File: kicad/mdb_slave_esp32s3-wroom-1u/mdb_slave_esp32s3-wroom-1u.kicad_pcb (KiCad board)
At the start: 2 copper layers, 127.5 x 79 mm, 66 parts, among them J1 USB_C_Receptacle_USB2.0_16P, J10 Conn_01x04_Pin_JST, J11 Screw_Terminal_01x03, J12 MDB_Connector, J13 Screw_Terminal_01x03, J14 Screw_Terminal_01x03, J2 Screw_Terminal_01x02, J3 Screw_Terminal_01x02, J4 Screw_Terminal_01x03, J5 Screw_Terminal_01x03, J6 Screw_Terminal_01x03, J7 Conn_01x06_Pin, J8 Conn_01x03_Pin_JST, J9 Conn_01x04_Pin, Q1 MMBT3904, Q2 MMBT3904, Q3 MMBT3904, SW1 SW_Push, U1 ESP32-S3-WROOM-1U-N16R2, U2 AP63203QWU-7, U3 TLP785, U4 TLP785

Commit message: fix(wroom-1u): correct board designator esp32s3-wroom-u1 -> esp32s3-wroom-1u
The module is actually named ESP32-S3-WROOM-1U, not "WROOM-U1" (digit/letter
order was swapped). Renames the KiCad project directory and its three
project files (.kicad_pro/.kicad_sch/.kicad_pcb), updates the embedded
project-name references inside them (sheet paths, instance paths), and
corrects the bottom-silkscreen text that gets printed on the physical board.
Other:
- board text added: "mdb-slave-esp32s3-wroom-1u"
- board text removed: "mdb-slave-esp32s3-wroom-u1"

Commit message: feat(wroom-1u): update PCB to rev1.2 (fully routed) and sync README
Board is now fully routed and fabrication-ready. README updated to
reflect rev1.2 status, the current connector reference designators
(J1-J3, P1-P8, H1), and functional blocks, replacing the stale
"not started" rev1.0 content and outdated J1-J14 connector table.
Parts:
- removed F1: 1.1A (33V), Fuse:Fuse_1812_4532Metric
- removed J10: Conn_01x04_Pin_JST, Connector_JST:JST_PH_B4B-PH-K_1x04_P2.00mm_Vertical
- removed J11, J13, J14, J4, J5, J6: Screw_Terminal_01x03, EasyEDA2Kicad:CONN-TH_3P-P2.54_DIBO_DB141R-2.54-3P
- removed J12: MDB_Connector, Connector_Molex:Molex_Mini-Fit_Jr_5566-06A_2x03_P4.20mm_Vertical
- removed J7: Conn_01x06_Pin, Connector_PinHeader_2.54mm:PinHeader_1x06_P2.54mm_Vertical
- removed J8: Conn_01x03_Pin_JST, Connector_JST:JST_PH_B3B-PH-K_1x03_P2.00mm_Vertical
- removed J9: Conn_01x04_Pin, Connector_PinHeader_2.54mm:PinHeader_1x04_P2.54mm_Vertical
- removed R23: 10k, Resistor_SMD:R_0603_1608Metric
- removed SW1: SW_Push, Button_Switch_SMD:SW_Tactile_SPST_NO_Straight_CK_PTS636Sx25SMTRLFS
- removed U2: AP63203QWU-7, Package_TO_SOT_SMD:TSOT-23-6
- removed U3, U4: TLP785, EasyEDA2Kicad:SMD-4_L4.6-W3.7-P2.54-LS7.0-BR
- added B1: Btn1, Global Libraries:KEY-SMD_B3U-1000PM, F.Cu at (85.3, 121.1)
- added B2: Btn1, Global Libraries:KEY-SMD_B3U-1000PM, F.Cu at (85.3, 124.2)
- added C10: 10uF, Capacitor_SMD:C_0603_1608Metric, F.Cu at (84.2, 141.5)
- added C11: 100nF, Capacitor_SMD:C_0603_1608Metric, F.Cu at (82.7, 141.5)
- added C12: 100nF, Capacitor_SMD:C_0603_1608Metric, F.Cu at (103.0, 136.2)
- added C7: 100nF, Capacitor_SMD:C_0603_1608Metric, F.Cu at (90.3, 148.9)
- added C8: 22uF, Capacitor_SMD:C_0603_1608Metric, F.Cu at (90.4, 142.3)
- added C9: 22uF, Capacitor_SMD:C_0603_1608Metric, F.Cu at (90.4, 140.8)
- added F2: Polyfuse, Capacitor_SMD:C_1812_4532Metric, F.Cu at (183.4, 143.5)
- added G***: LOGO, LOGO, B.Cu at (92.5, 122.0)
- added H10: Buzzer_OUT, TestPoint:TestPoint_Pad_D1.0mm, B.Cu at (127.7, 134.6)
- added H6: +5V, TestPoint:TestPoint_Pad_D1.0mm, B.Cu at (82.5, 141.6)
- added H7: +3V3, TestPoint:TestPoint_Pad_D1.0mm, B.Cu at (89.8, 144.8)
- added H8: DO, TestPoint:TestPoint_Pad_D1.0mm, F.Cu at (109.1, 136.2)
- added H9: Buzzer_IN, TestPoint:TestPoint_Pad_D1.0mm, B.Cu at (113.2, 136.2)
- added LED1: XL-2121RGBC-2812B, Global Libraries:LED-SMD_4P-L2.1-W2.1-BR_XL-2121RGBC-WS2812B_C5349957, F.Cu at (106.2, 135.7)
- added P1: WJ500V-5.08-3P-14-00A, Global Libraries:CONN-TH_3P-P5.00_WJ500V-5.08-3P_C72334, F.Cu at (183.5, 118.6)
- added P2: WJ500V-5.08-3P-14-00A, Global Libraries:CONN-TH_3P-P5.00_WJ500V-5.08-3P_C72334, F.Cu at (168.0, 118.6)
- added P3: WJ500V-5.08-3P-14-00A, Global Libraries:CONN-TH_3P-P5.00_WJ500V-5.08-3P_C72334, F.Cu at (147.8, 145.9)
- added P4: WJ500V-5.08-3P-14-00A, Global Libraries:CONN-TH_3P-P5.00_WJ500V-5.08-3P_C72334, F.Cu at (101.2, 145.9)
- added P5: WJ500V-5.08-3P-14-00A, Global Libraries:CONN-TH_3P-P5.00_WJ500V-5.08-3P_C72334, F.Cu at (116.7, 145.9)
- added P6: WJ500V-5.08-3P-14-00A, Global Libraries:CONN-TH_3P-P5.00_WJ500V-5.08-3P_C72334, F.Cu at (132.3, 145.9)
- added P7: WJ500V-5.08-2P-14-00A, Global Libraries:CONN-TH_2P-P5.00_WJ500V-5.08-2P_C8465, F.Cu at (196.5, 128.1)
- added P8: WJ500V-5.08-2P-14-00A, Global Libraries:CONN-TH_2P-P5.00_WJ500V-5.08-2P_C8465, F.Cu at (196.5, 138.6)
- added U5: TLP785, Global Libraries:SMD-4_L4.6-W6.5-P2.54-LS10.2-BR_C45445, F.Cu at (138.5, 134.2)
- added U6: TLP785, Global Libraries:SMD-4_L4.6-W6.5-P2.54-LS10.2-BR_C45445, F.Cu at (138.5, 127.6)
- added U8: AP63203QWU-7, Package_TO_SOT_SMD:TSOT-23-6, F.Cu at (88.7, 145.3)
- added USBC1: TYPE-C-31-M-12, Global Libraries:USB-C_SMD-TYPE-C-31-M-12, F.Cu at (83.3, 131.9)
- BUZZER1: footprint easyeda2kicad:BUZ-SMD_4P-L8.5-W8.5-P8.50-BR -> Global Libraries:BUZ-SMD_4P-L8.5-W8.5-P8.50-BR_C94599
- C5: value 22uF -> 100nF
- C6: value 22uF -> 10uF
- D1: value Schottky 60V/1A -> 1N4148WS; footprint Diode_SMD:D_SOD-123 -> Diode_SMD:D_SOD-323
- D2: value XL-2121RGBC-2812B -> 1N4148WS; footprint LED_SMD:LED_WS2812B-2020_PLCC4_2.0x2.0mm -> Diode_SMD:D_SOD-323
- D3: value Schottky 30V/500mA -> BAT760-7; footprint Diode_SMD:D_SOD-123 -> Diode_SMD:D_SOD-323
- D4: value Schottky 30V/500mA -> 1N4148WS; footprint Diode_SMD:D_SOD-123 -> Diode_SMD:D_SOD-323
- D5, D6: value 1N4148WS -> BAT760-7
- H1: value MountingHole2.5 -> HC-5557-2*3AW; footprint MountingHole:MountingHole_2.5mm -> Global Libraries:CONN-TH_6P-P4.20-S5.50_5557-2X3AW_C2845788
- H2, H3, H4, H5: value MountingHole2.5 -> MountingHole; footprint MountingHole:MountingHole_2.5mm -> MountingHole:MountingHole_2.7mm_M2.5_ISO7380
- J1: value USB_C_Receptacle_USB2.0_16P -> Conn_01x06_Pin; footprint Connector_USB:USB_C_Receptacle_G-Switch_GT-USB-7010ASV -> Connector_PinSocket_2.54mm:PinSocket_1x06_P2.54mm_Vertical
- J2: value Screw_Terminal_01x02 -> Conn_01x06_Pin; footprint EasyEDA2Kicad:CONN-TH_2P-P2.54_DIBO_DB141R-2.54-2P -> Connector_PinSocket_2.54mm:PinSocket_1x06_P2.54mm_Vertical
- J3: value Screw_Terminal_01x02 -> Conn_01x04_Pin; footprint EasyEDA2Kicad:CONN-TH_2P-P2.54_DIBO_DB141R-2.54-2P -> Connector_JST:JST_XH_B4B-XH-A_1x04_P2.50mm_Vertical
- L1: footprint Inductor_SMD:L_TechFuse_SL0420 -> Inductor_SMD:L_0603_1608Metric
- R1, R17, R2: value 10k -> 10KΩ
- R10, R20: value 1k -> 10KΩ
- R11, R8: value 4.7k -> 4.7KΩ
- R12: value 100ohm -> 470Ω
- R13: value 4.7k -> 10KΩ
- R14, R15: value 4.7k -> 1KΩ
- R16: value 4.7k -> 470Ω
- R18: value 470ohm -> 10KΩ
- R19: value 10k -> 1KΩ
- R21: value 470ohm -> 5.1KΩ
- R22: value 10k -> 5.1KΩ
- R3: value 5.1k -> 470Ω
- R4: value 5.1k -> 4.7KΩ
- R5, R6: value 10k -> 0R; footprint Resistor_SMD:R_0603_1608Metric -> Resistor_SMD:R_0603_1608Metric_Pad0.98x0.95mm_HandSolder
- R7: value 10k -> 4.7KΩ
- R9: value 1k -> 4.7KΩ
- TH1: footprint Resistor_SMD:R_0603_1608Metric -> Capacitor_SMD:C_0603_1608Metric_Pad1.08x0.95mm_HandSolder
- U1: footprint EasyEDA2Kicad:WIRELM-SMD_ESP32-S3-WROOM-1U -> Global Libraries:WIRELM-SMD_ESP32-S3-WROOM-1U_C3013945
- moved H3 263.5 mm to (82.5, 116.5)
- moved H2 245.7 mm to (82.5, 148.0)
- moved D6 162.2 mm to (85.9, 141.6), turned to 90 degrees
- moved H5 148.1 mm to (198.8, 116.5)
- moved H1 142.3 mm to (170.9, 135.0)
- moved H4 134.5 mm to (198.8, 148.0)
- moved R17 123.5 mm to (177.5, 124.9), turned to 180 degrees
- moved R19 115.1 mm to (180.6, 130.5), turned to -90 degrees
- moved Q1 111.7 mm to (128.9, 130.6), turned to -90 degrees
- moved D1 108.4 mm to (120.3, 134.6)
- moved L1 103.4 mm to (88.7, 148.9), turned to -90 degrees
- moved BUZZER1 99.9 mm to (120.4, 127.9)
- moved R9 96.7 mm to (152.9, 120.8), turned to 180 degrees
- moved C6 96.5 mm to (87.8, 141.6), turned to 90 degrees
- moved J1 95.3 mm to (114.4, 114.8), turned to 90 degrees
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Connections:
- net /io6 renamed GPIO6
- BUZZER1 pad 2: GND -> Net-(BUZZER1-Pad2)
- C1 pad 1: GND -> EN
- C1 pad 2: +3V3 -> GND
- C3 pad 1: /vin -> GND
- C3 pad 2: Net-(U2-IN) -> +3V3
- C4 pad 1: Net-(U2-BST) -> EN
- C4 pad 2: Net-(U2-SW) -> GND
- C5 pad 1: +3V3 -> IO0
- C6 pad 1: +3V3 -> +5V
- D1 pad 1: /vin -> +3V3
- D2 pad 1: unconnected-(D2-DOUT-Pad1) -> Net-(D2-K)
- D2 pad 2: GND -> Net-(D2-A)
- D4 pad 1: +3V3 -> Net-(D4-K)
- D5 pad 1: Net-(D5-K) -> +3V3
- D6 pad 1: Net-(D6-K) -> +5V
- J2 pad 1: Net-(D3-A) -> /MTMS
- J2 pad 2: +3V3 -> /MTDI
- J3 pad 1: Net-(D4-A) -> GND
- L1 pad 1: Net-(U2-SW) -> Net-(U8-SW)
- Q1 pad 3: Net-(D3-A) -> Net-(D1-A)
- Q2 pad 3: Net-(D4-A) -> Net-(D3-A)
- Q3 pad 3: Net-(J8-Pin_3) -> Net-(D5-A)
- R1 pad 1: /boot -> +3V3
- R1 pad 2: +3V3 -> EN
- R10 pad 1: Net-(Q2-B) -> +3V3
- R10 pad 2: /io2 -> IO0
- R11 pad 2: /io15 -> GPIO15
- R12 pad 1: Net-(BUZZER1-+) -> /mdb_master_transmit
- R12 pad 2: /io12 -> Net-(D2-A)
- R13 pad 1: /io16 -> GPIO7
- R14 pad 1: /io13 -> +3V3
- R14 pad 2: Net-(Q3-B) -> GPIO4
- R15 pad 1: /io11 -> Net-(Q2-B)
- R15 pad 2: +3V3 -> GPIO2
- R16 pad 1: /io10 -> Net-(D4-A)
- R18 pad 1: Net-(D5-A) -> GPIO17
- R18 pad 2: /mdb_master_transmit -> +3V3
- R19 pad 1: /io47 -> Net-(Q3-B)
- R19 pad 2: +3V3 -> GPIO1
- R2 pad 1: +3V3 -> Net-(U1-IO3)
- R2 pad 2: Net-(U1-EN) -> GND
- R20 pad 1: +3V3 -> GPIO18
- R20 pad 2: /io4 -> +3V3
- R21 pad 1: +3V3 -> Net-(USBC1-CC1)
- R21 pad 2: Net-(D6-A) -> GND
- R22 pad 1: /io48 -> Net-(USBC1-CC2)
- R22 pad 2: +3V3 -> GND
- R3 pad 1: Net-(J1-CC2) -> GPIO12
- R3 pad 2: GND -> Net-(Q1-B)
- R4 pad 1: Net-(J1-CC1) -> +3V3
- R4 pad 2: GND -> GPIO15
- R5 pad 1: Net-(U1-IO46) -> +3V3
- R5 pad 2: GND -> Net-(BUZZER1-+)
- R6 pad 1: Net-(U1-IO45) -> Net-(D1-A)
- R6 pad 2: GND -> Net-(BUZZER1-Pad2)
- R7 pad 1: /io7 -> +3V3
- R7 pad 2: +3V3 -> GPIO16
- R8 pad 1: /io15 -> GPIO10_SDA
- R9 pad 1: Net-(Q1-B) -> GPIO11_SCL
- R9 pad 2: /io1 -> +3V3
- TH1 pad 1: GND -> GPIO7
- TH1 pad 2: /io7 -> GND
- U1 pad 10: unconnected-(U1-IO17-Pad10) -> GPIO17
- U1 pad 11: unconnected-(U1-IO18-Pad11) -> GPIO18
- U1 pad 13: /usb- -> USB_D-
- U1 pad 14: /usb+ -> USB_D+
- U1 pad 16: Net-(U1-IO46) -> unconnected-(U1-IO46-Pad16)
- U1 pad 18: /io10 -> GPIO10_SDA
- U1 pad 19: /io11 -> GPIO11_SCL
- U1 pad 20: /io12 -> GPIO12
- U1 pad 21: /io13 -> unconnected-(U1-IO13-Pad21)
- U1 pad 23: /io21 -> GPIO21
- U1 pad 24: /io47 -> unconnected-(U1-IO47-Pad24)
- U1 pad 25: /io48 -> unconnected-(U1-IO48-Pad25)
- U1 pad 26: Net-(U1-IO45) -> unconnected-(U1-IO45-Pad26)
- U1 pad 27: /boot -> IO0
- U1 pad 3: Net-(U1-EN) -> EN
- U1 pad 32: /io39 -> /MTCk
- U1 pad 33: /io40 -> /MTDO
- U1 pad 34: /io41 -> /MTDI
- U1 pad 35: /io42 -> /MTMS
- U1 pad 36: /u0rxd -> /RXD
- U1 pad 37: /u0txd -> /TXD
- U1 pad 38: /io2 -> GPIO2
- U1 pad 39: /io1 -> GPIO1
- U1 pad 4: /io4 -> GPIO4
- U1 pad 5: /io5 -> GPIO5
- U1 pad 7: /io7 -> GPIO7
- U1 pad 8: /io15 -> GPIO15
- U1 pad 9: /io16 -> GPIO16
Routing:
- net +3V3: track 0.00 -> 436.9 mm, vias 0 -> 9
- net +5V: track 0.00 -> 120.8 mm, vias 0 -> 2
- net GPIO6: track 0.00 -> 116.0 mm, vias 0 -> 1
- net GPIO15: track 0.00 -> 100.2 mm, vias 0 -> 2
- net GPIO17: track 0.00 -> 98.8 mm, vias 0 -> 2
- net GPIO18: track 0.00 -> 89.5 mm, vias 0 -> 2
- net GPIO10_SDA: track 0.00 -> 82.8 mm, vias 0 -> 2
- net GPIO2: track 0.00 -> 80.8 mm, vias 0 -> 2
- net GPIO11_SCL: track 0.00 -> 77.6 mm, vias 0 -> 2
- net GPIO1: track 0.00 -> 75.8 mm, vias 0 -> 2
- net IO0: track 0.00 -> 64.5 mm, vias 0 -> 4
- net /mdb_master_receive: track 0.00 -> 58.0 mm
- net /mdb_communications_common: track 0.00 -> 55.8 mm
- net GPIO5: track 0.00 -> 52.2 mm, vias 0 -> 2
- net GPIO4: track 0.00 -> 50.9 mm, vias 0 -> 2
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- added copper zone on B.Cu, net GND
- added copper zone on F.Cu, net GND
- added copper zone on In1.Cu, net GND
- added copper zone on In2.Cu, net GND
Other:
- board size 127.5 x 79 mm -> 123.2 x 38.5 mm
- copper layers 2 -> 4
- board text added: "0/BOOT"
- board text added: "1-WIRE BUS#1"
- board text added: "1-WIRE BUS#2"
- board text added: "123.2 mm"
- board text added: "38.5 mm"
- board text added: "3V3"
- board text added: "3v3"
- board text added: "5V"
- board text added: "Buzzer OUT"
- board text added: "CUST. IN #1"
- board text added: "CUST. IN #2"
- board text added: "CUST. IN #3"
- board text added: "EN"
- board text added: "GND"
- board text added: "GPIO15"
- board text added: "GPIO16"
- board text added: "GPIO17"
- board text added: "GPIO18"
- board text added: "GPIO6"
- board text added: "I2C"
- board text added: "IN"
- board text added: "IO0"
- board text added: "JTAG"
- board text added: "LED DO"
- board text added: "MDB"
- board text added: "MDB-ESP32-CASHLESS WROOM-1U BOARD"
- board text added: "MD_C"
- board text added: "MD_R"
- board text added: "MD_T"
- board text added: "MTCK"
- board text added: "MTDI"
- board text added: "MTDO"
- board text added: "MTMS"
- board text added: "RELAY #1"
- board text added: "RELAY #2"
- board text added: "REV 1.2"
- board text added: "RST"
- board text added: "RXD"
- board text added: "SCL"
- board text added: "SDA"
- board text added: "TXD"
- board text added: "UART DEBUG"
- board text added: "VIN"
- board text added: "X"
- board text removed: "commit xxxxxxx"
- board text removed: "mdb-slave-esp32s3-wroom-1u"

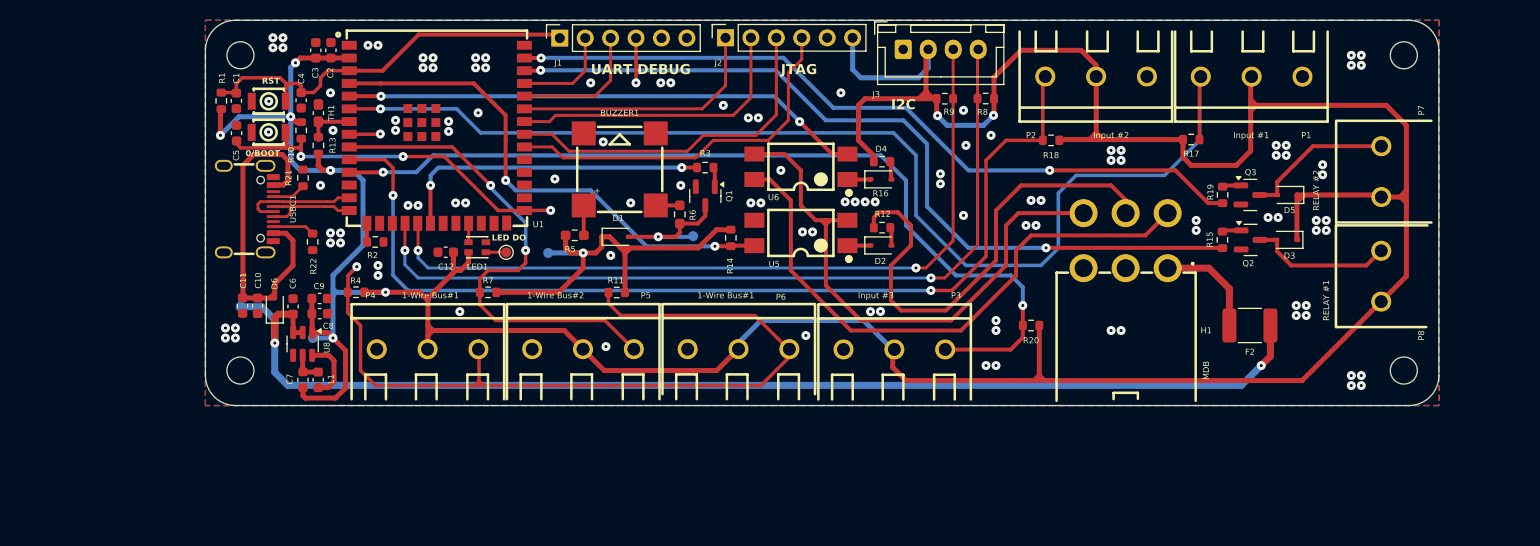
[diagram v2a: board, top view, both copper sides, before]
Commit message: feat(wroom-1u): update PCB to rev1.3 (15A relay upgrade) and add fabrication gerbers
- Relay outputs redesigned: SRD-03VDC-SL-C 15A-class relays (K2/K3) driven
  low-side by MMBT3904 (Q2/Q3) with 1N4148WS flyback diodes, switched
  through TLP785 optocouplers (U4/U5) for GPIO isolation
- README rewritten to match rev1.3: updated reference designators, honest
  status section (4 minor ERC items, PCB/schematic re-sync pending),
  known relay drive-logic inversion documented as an open point
- Add gerber_to_order/ (JLCPCB, PCBWay) fabrication archives, versioned via
  .gitignore whitelist update

Note: PCB/schematic parity re-sync (reference renumbering from the relay
stage addition) and a voltage regulator issue are still open, handed off
to the hardware engineer for follow-up before ordering.
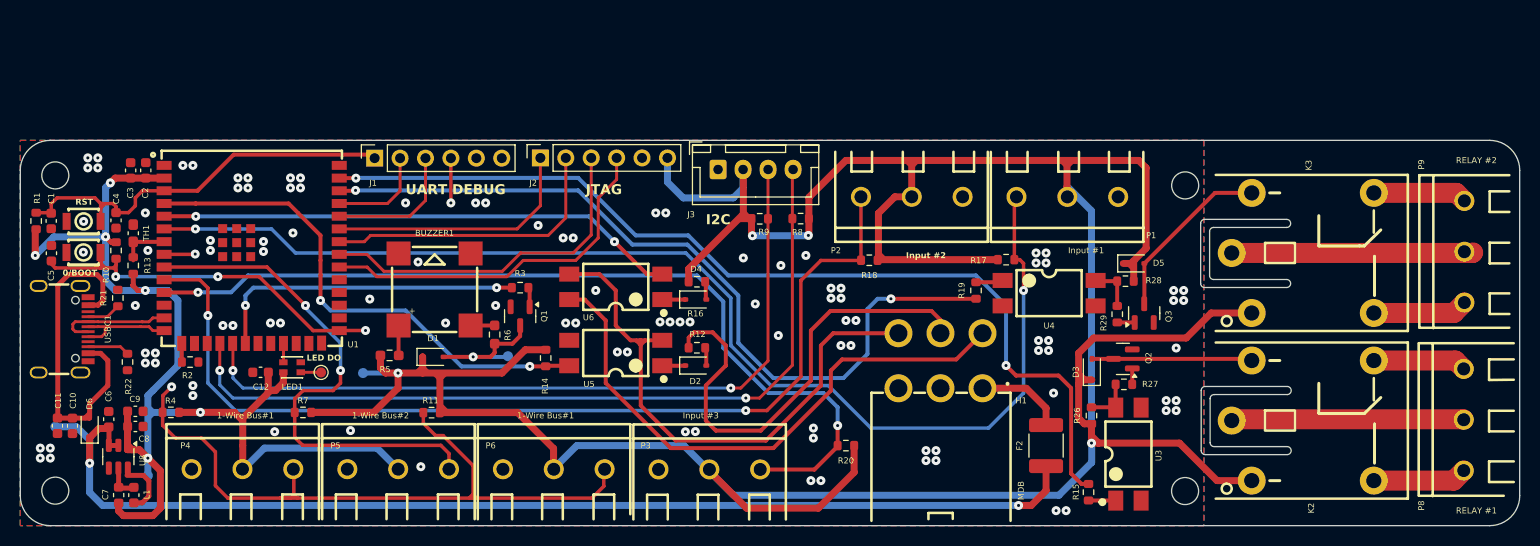
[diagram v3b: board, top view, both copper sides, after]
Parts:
- removed P7: WJ500V-5.08-2P-14-00A, Global Libraries:CONN-TH_2P-P5.00_WJ500V-5.08-2P_C8465
- added K2: SRD-03VDC-SL-C, Global Libraries:RELAY-TH_SRD-XXVDC-XL-C_C24585, F.Cu at (188.6, 153.0)
- added K3: SRD-03VDC-SL-C, Global Libraries:RELAY-TH_SRD-XXVDC-XL-C_C24585, F.Cu at (188.6, 136.3)
- added P9: WJ500V-5.08-3P-14-00A, Global Libraries:CONN-TH_3P-P5.00_WJ500V-5.08-3P_C72334, F.Cu at (204.8, 136.1)
- added R26: 10KΩ, Resistor_SMD:R_0603_1608Metric, F.Cu at (167.5, 152.5)
- added R27: 100Ω, Resistor_SMD:R_0603_1608Metric, F.Cu at (170.8, 149.4)
- added R28: 10KΩ, Resistor_SMD:R_0603_1608Metric, F.Cu at (170.9, 139.1)
- added R29: 100Ω, Resistor_SMD:R_0603_1608Metric, F.Cu at (170.1, 142.4)
- added U3: TLP785, Global Libraries:SMD-4_L4.6-W6.5-P2.54-LS10.2-BR_C45445, F.Cu at (171.2, 156.3)
- added U4: TLP785, Global Libraries:SMD-4_L4.6-W6.5-P2.54-LS10.2-BR_C45445, F.Cu at (163.3, 140.3)
- D3, D5: value BAT760-7 -> 1N4148WS
- P8: value WJ500V-5.08-2P-14-00A -> WJ500V-5.08-3P-14-00A; footprint Global Libraries:CONN-TH_2P-P5.00_WJ500V-5.08-2P_C8465 -> Global Libraries:CONN-TH_3P-P5.00_WJ500V-5.08-3P_C72334
- R15, R19: value 1KΩ -> 270Ω
- moved R15 28.5 mm to (167.2, 160.2)
- moved R19 26.4 mm to (156.0, 140.0), turned to 90 degrees
- moved H5 25.4 mm to (176.9, 129.5)
- moved H4 25.0 mm to (176.9, 160.0)
- moved F2 23.6 mm to (163.0, 155.5), turned to 90 degrees
- moved D3 23.4 mm to (167.6, 147.9), turned to 90 degrees
- moved G*** 23.4 mm to (72.8, 134.6)
- moved R3 22.1 mm to (110.4, 139.7)
- moved BUZZER1 22.1 mm to (101.9, 139.9)
- moved C3 22.1 mm to (71.5, 128.0)
- moved R17 22.1 mm to (159.0, 136.9)
- moved R9 22.1 mm to (134.4, 132.8)
- moved U1 22.1 mm to (83.6, 136.4)
- moved B1 22.1 mm to (66.8, 133.1)
- moved C10 22.1 mm to (65.7, 153.5)
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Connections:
- P8 pad 1: Net-(D3-A) -> Net-(K2-Pad2)
- P8 pad 2: +3V3 -> Net-(K2-Pad5)
- R15 pad 1: Net-(Q2-B) -> GPIO1
- R15 pad 2: GPIO2 -> Net-(R15-Pad2)
- R19 pad 1: Net-(Q3-B) -> GPIO2
- R19 pad 2: GPIO1 -> Net-(R19-Pad2)
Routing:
- net +3V3: track 436.9 -> 482.0 mm, vias 9 -> 10
- net Net-(K3-Pad5): track 0.00 -> 24.1 mm
- net Net-(K2-Pad5): track 0.00 -> 23.2 mm
- net GPIO1: track 75.8 -> 96.1 mm
- net GPIO15: track 100.2 -> 89.6 mm
- net Net-(K3-Pad2): track 0.00 -> 9.48 mm
- net Net-(K2-Pad2): track 0.00 -> 9.40 mm
- net Net-(K3-Pad3): track 0.00 -> 9.38 mm
- net Net-(K2-Pad3): track 0.00 -> 9.33 mm
- net +5V: track 120.8 -> 116.1 mm
- net Net-(R26-Pad2): track 0.00 -> 4.71 mm
- net Net-(R28-Pad2): track 0.00 -> 4.56 mm
- net Net-(D5-A): track 14.9 -> 17.7 mm
- net GPIO6: track 116.0 -> 118.7 mm, vias 1 -> 2
- net Net-(R15-Pad2): track 0.00 -> 2.70 mm
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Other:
- board size 123.2 x 38.5 mm -> 149.8 x 38.5 mm
- board text added: "149.7 mm"
- board text added: "NC"
- board text added: "NO"
- board text added: "REV 1.3"
- board text removed: "123.2 mm"
- board text removed: "IN"
- board text removed: "REV 1.2"

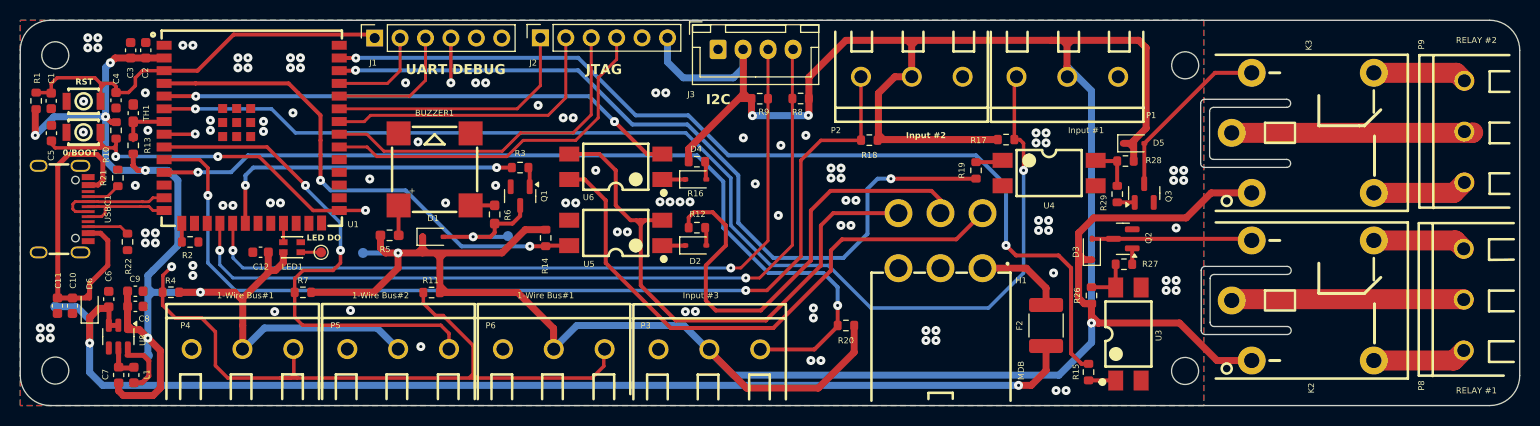
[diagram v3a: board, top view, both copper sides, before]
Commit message: feat(wroom-1u): update PCB to rev1.4 (adjustable buck + schematic re-sync)
Swap U8 buck regulator from fixed-output AP63203QWU-7 to adjustable
AP63201WU-7, with a new external feedback divider (R23 196k / R24 62k)
and feed-forward cap (C19 100pF) to set the 3.3V rail.

Complete the schematic/PCB re-sync left open in rev1.3: the orphaned
1-Wire pull-up (R4) is now properly linked, and all connector/optocoupler
references have been renumbered and re-annotated consistently across
schematic and PCB (P1-P9, H1-H10, U3/U5/U6). Fix an accidental sheet
label ("mdb_slave_sharnobile" -> "mdb_slave_esp32s3-wroom-1u") picked up
during the KiCad resync. Regenerate gerbers for JLCPCB/PCBWay.

README updated to match: rev1.4, new buck part/feedback network, and all
renumbered connector references.
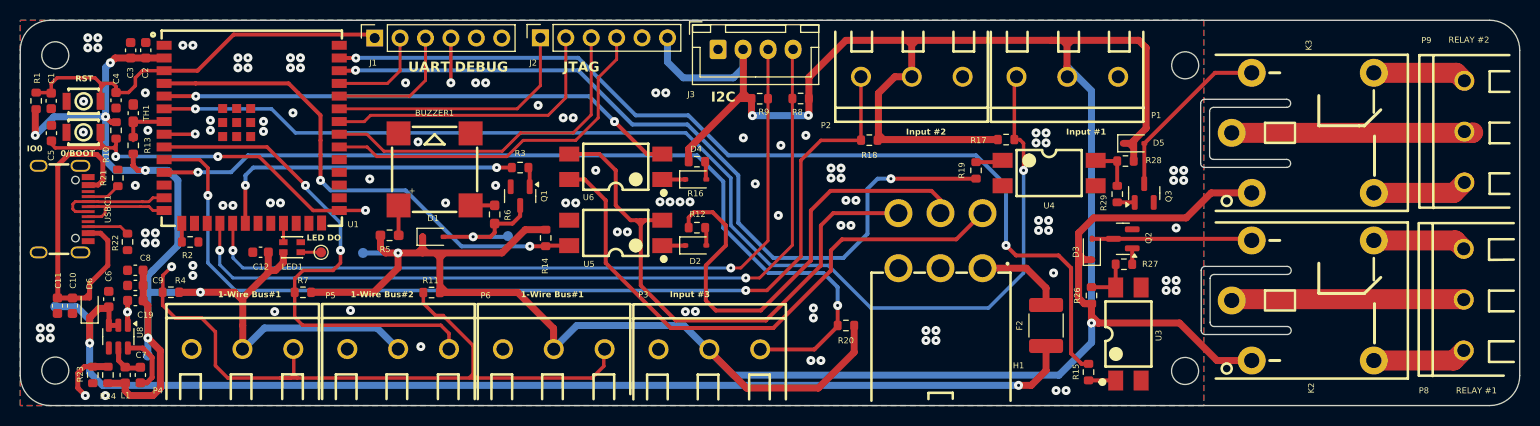
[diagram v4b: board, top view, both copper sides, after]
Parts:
- added C19: 100pF, Capacitor_SMD:C_0603_1608Metric, F.Cu at (72.0, 153.0)
- added R23: 196KΩ, Resistor_SMD:R_0603_1608Metric, F.Cu at (69.3, 160.4)
- added R24: 62KΩ, Resistor_SMD:R_0603_1608Metric, F.Cu at (67.7, 160.4)
- U8: value AP63203QWU-7 -> AP63201WU-7
- moved C8 3.61 mm to (72.0, 150.0), turned to 0 degrees
- moved G*** 1.34 mm to (74.0, 134.0)
- moved C7 0.65 mm to (72.5, 160.4)
- moved L1 0.65 mm to (71.0, 160.4)
- moved C9 0.58 mm to (72.0, 151.5), turned to 0 degrees
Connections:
- U8 pad 1: +3V3 -> Net-(U8-FB)
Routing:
- net Net-(U8-FB): track 0.00 -> 18.7 mm, vias 0 -> 2
- net Net-(U8-SW): track 3.14 -> 3.66 mm
- net GND: vias 105 -> 106
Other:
- board text added: "1-Wire Bus#1"
- board text added: "1-Wire Bus#2"
- board text added: "Input #1"
- board text added: "Input #2"
- board text added: "Input #3"
- board text added: "REV 1.4"
- board text removed: "REV 1.3"
